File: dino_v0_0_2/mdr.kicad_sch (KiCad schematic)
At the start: 12 parts, among them U18 74LS373, U22 74LS02, U25 74LS245, U34 74LS373, U37 74LS04, U39 74LS00

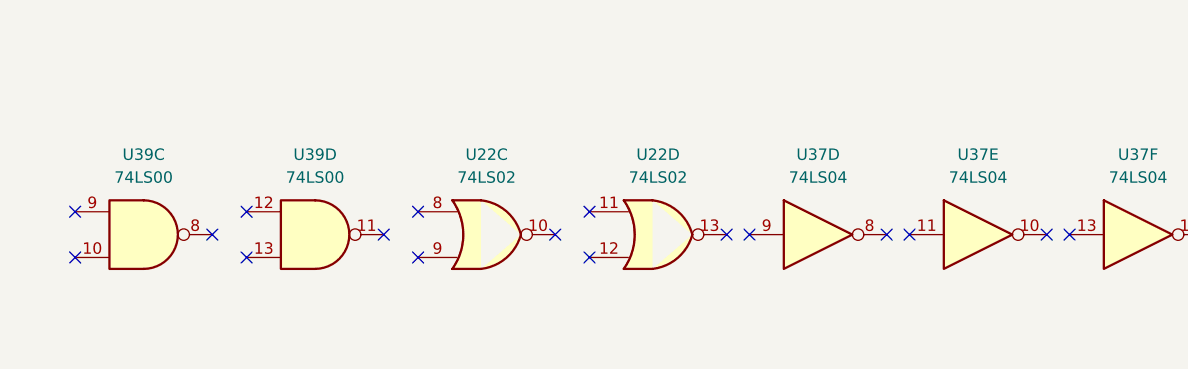
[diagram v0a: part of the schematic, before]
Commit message: feat(dino): generate + stamp per-sheet I/O contracts
Each module's boundary signals (IN/OUT/BIDIR with counterpart sheets)
derived from the kicad-cli netlist and placed as a text block on the
physical sheet, so a bench rig knows exactly what to drive and observe
per board. kicad_contracts.py regenerates both the markdown and the
stamps idempotently; stamping verified electrically neutral.
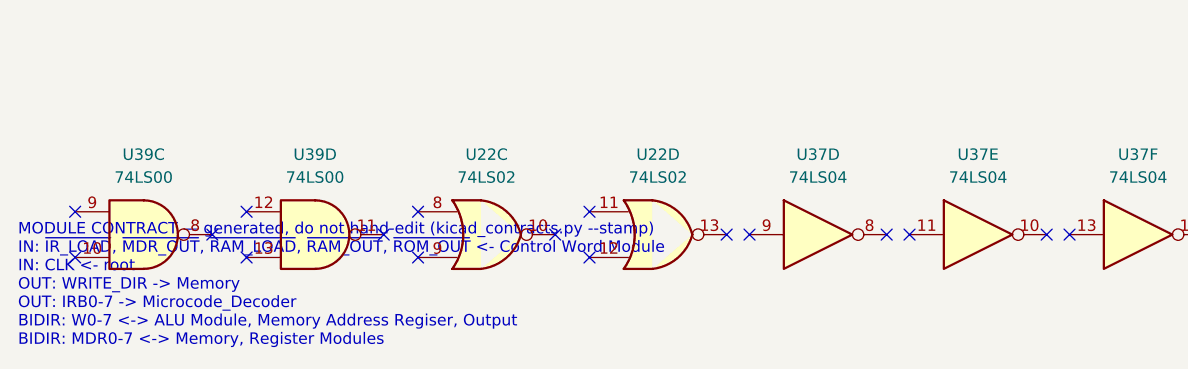
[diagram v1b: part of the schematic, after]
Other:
- note added: "MODULE CONTRACT — generated, do not hand-edit (kicad_contracts.py --stamp) IN: ~{IR_LOAD}, ~{MDR_OUT}, ~{RAM_LOAD}, ~{RAM_OUT}, ~{ROM_OUT} <- Control Word Module IN: CLK <- root OUT: WRITE_DIR -> Memory OUT: IRB0-7 -> Microcode_Decoder BIDIR: W0-7 <-> ALU Module, Memory Address Regiser, Output BIDIR: MDR0-7 <-> Memory, Register Modules"
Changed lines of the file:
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@@
+		)
+	)
+	(text "MODULE CONTRACT — generated, do not hand-edit (kicad_contracts.py --stamp)\nIN: ~{IR_LOAD}, ~{MDR_OUT}, ~{RAM_LOAD}, ~{RAM_OUT}, ~{ROM_OUT} <- Control Word Module\nIN: CLK <- root\nOUT: WRITE_DIR -> Memory\nOUT: IRB0-7 -> Microcode_Decoder\nBIDIR: W0-7 <-> ALU Module, Memory Address Regiser, Output\nBIDIR: MDR0-7 <-> Memory, Register Modules"
+		(exclude_from_sim no)
+		(at 15.24 208.12 0)
+		(effects
+			(font
+				(size 1.27 1.27)
+			)
+			(justify left bottom)
 		)
 	)
